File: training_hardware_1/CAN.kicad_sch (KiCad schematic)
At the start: 7 parts, among them U2 OKI

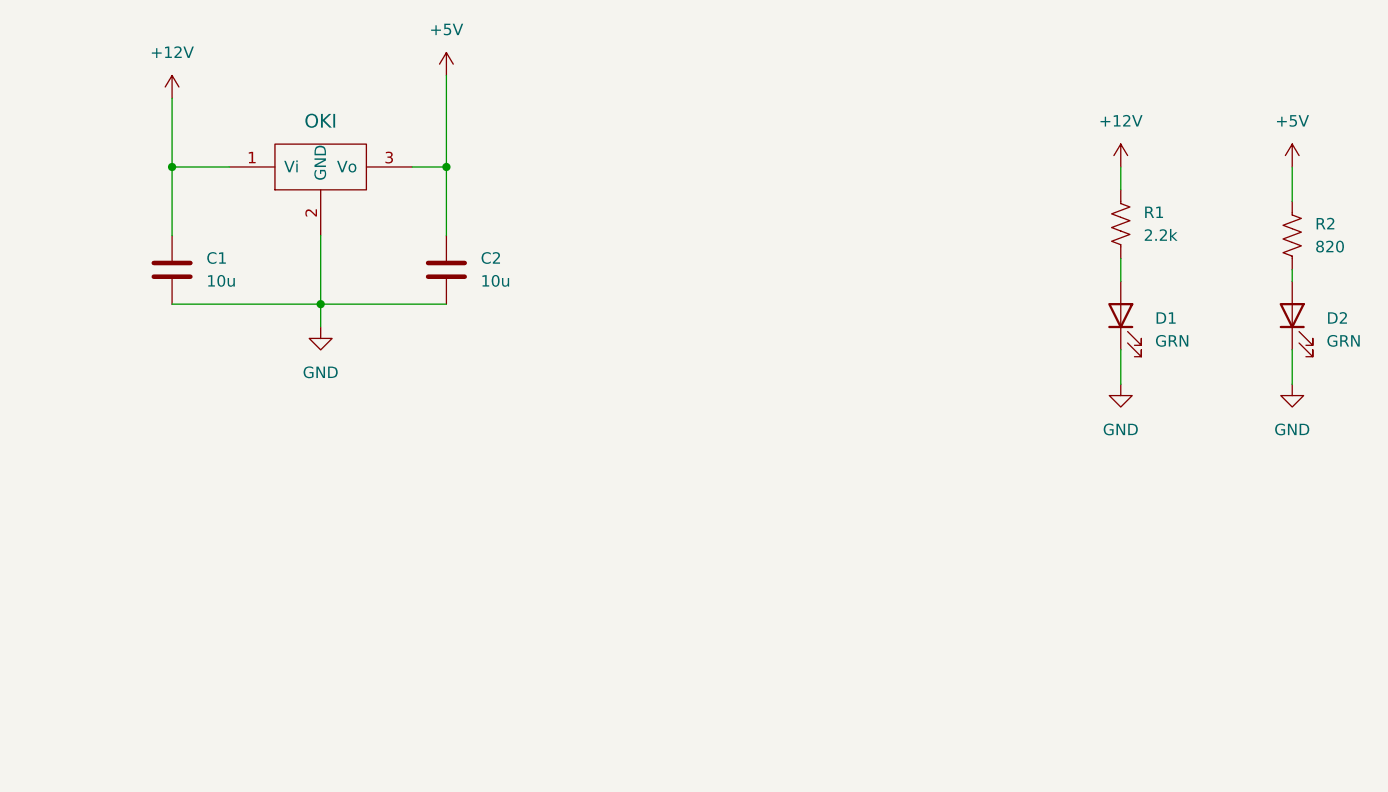
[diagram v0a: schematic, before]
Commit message: Add CAN Transceiver
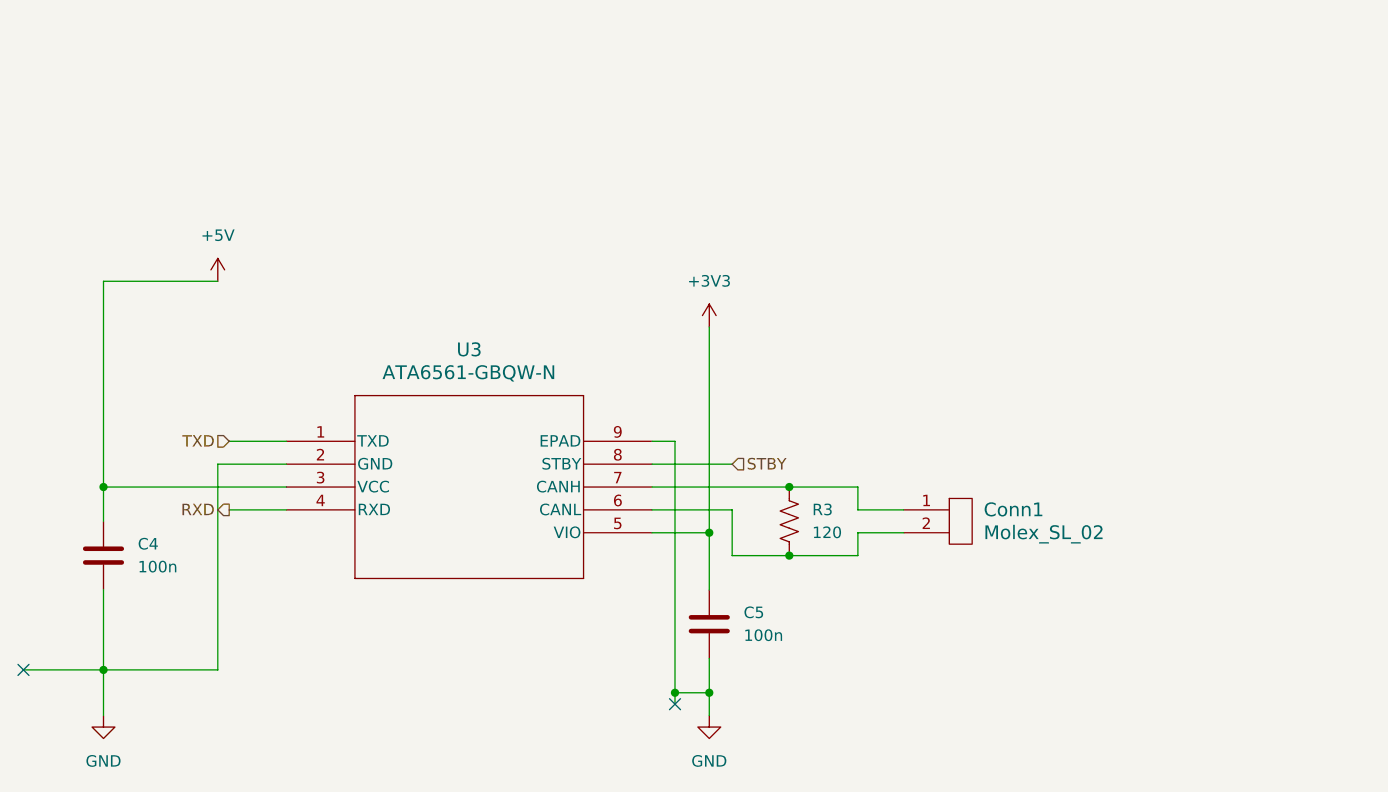
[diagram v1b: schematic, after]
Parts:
- removed C1, C2: 10u, symbol Device:C
- removed D1, D2: GRN, symbol Device:LED
- removed R1: 2.2k, symbol Device:R_US
- removed R2: 820, symbol Device:R_US
- removed U2: OKI, symbol MRDT_Devices:OKI
- added C4, C5: 100n, symbol Device:C
- added Conn1: Molex_SL_02, symbol MRDT_Connectors:Molex_SL_02
- added R3: 120, symbol Device:R_US
- added U3: ATA6561-GBQW-N, VDFN8_3X3_MCH, symbol 2026_training_hardware:ATA6561-GBQW-N
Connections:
- net +5V: now also C4.1, U3.3 (VCC)
- net GND: now also C4.2, C5.2, U3.2 (GND), U3.9 (EPAD)
- new net: Conn1.2, R3.2, U3.6 (CANL)
- new net: Conn1.1, R3.1, U3.7 (CANH)
- new net +3V3: C5.1, U3.5 (VIO)
- new net RXD: U3.4 (RXD)
- new net STBY: U3.8 (STBY)
- new net TXD: U3.1 (TXD)
- no-connect marks 0 -> 2

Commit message: 11:34 in
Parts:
- C4, C5: footprint (none) -> Capacitor_SMD:C_0603_1608Metric_Pad1.08x0.95mm_HandSolder
- R3: footprint (none) -> Resistor_SMD:R_0603_1608Metric_Pad0.98x0.95mm_HandSolder
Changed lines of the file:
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@@
 			)
 		)
-		(property "Footprint" ""
+		(property "Footprint" "Capacitor_SMD:C_0603_1608Metric_Pad1.08x0.95mm_HandSolder"
 			(at 145.7452 116.84 0)
 			(effects
@@
 			)
 		)
-		(property "Footprint" ""
+		(property "Footprint" "Capacitor_SMD:C_0603_1608Metric_Pad1.08x0.95mm_HandSolder"
 			(at 78.4352 109.22 0)
 			(effects
@@
 			)
 		)
-		(property "Footprint" ""
+		(property "Footprint" "Resistor_SMD:R_0603_1608Metric_Pad0.98x0.95mm_HandSolder"
 			(at 154.686 101.854 90)
 			(effects

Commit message: Add components and wires(1:28)
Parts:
- removed U3: ATA6561-GBQW-N, VDFN8_3X3_MCH, symbol 2026_training_hardware:ATA6561-GBQW-N
- added U3: ATA6561-GAQW-N, 2026_Training_Hardware:SOIC8_4P9X3P9MC_MCH-L, symbol 2026_training_hardware:ATA6561-GAQW-N
- Conn1: footprint (none) -> MRDT_Connectors:MOLEX_SL_02_Vertical
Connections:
- net +3V3: now also U3.5 (VIO)
- net +5V: now also U3.3 (VCC)
- net GND: now also U3.2 (GND), U3.9 (EPAD)
- net RXD: now also U3.4 (RXD)
- net STBY: now also U3.8 (STBY)
- net TXD: now also U3.1 (TXD)
- net at Conn1.2, R3.2: now also U3.6 (CANL)
- net at Conn1.1, R3.1: now also U3.7 (CANH)
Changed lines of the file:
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@@
 	)
 	(symbol
-		(lib_id "2026_training_hardware:ATA6561-GBQW-N")
+		(lib_id "2026_training_hardware:ATA6561-GAQW-N")
 		(at 97.79 92.71 0)
 		(unit 1)
@@
 			)
 		)
-		(property "Value" "ATA6561-GBQW-N"
+		(property "Value" "ATA6561-GAQW-N"
 			(at 118.11 85.09 0)
 			(effects
@@
 			)
 		)
-		(property "Footprint" "VDFN8_3X3_MCH"
+		(property "Footprint" "2026_Training_Hardware:SOIC8_4P9X3P9MC_MCH-L"
 			(at 97.79 92.71 0)
 			(effects
@@
 			)
 		)
+		(pin "3"
+		)
+		(pin "1"
+		)
+		(pin "4"
+		)
+		(pin "7"
+		)
 		(pin "5"
+		)
+		(pin "2"
+		)
+		(pin "8"
 		)
 		(pin "9"
 		)
-		(pin "7"
-		)
-		(pin "1"
-		)
 		(pin "6"
-		)
-		(pin "2"
-		)
-		(pin "3"
-		)
-		(pin "4"
-		)
-		(pin "8"
 		)
 		(instances
@@
 			)
 		)
-		(property "Footprint" ""
+		(property "Footprint" "MRDT_Connectors:MOLEX_SL_02_Vertical"
 			(at 171.45 106.68 0)
 			(effects
